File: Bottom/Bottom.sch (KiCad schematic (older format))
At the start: 41 parts, among them M1 Stepper_Motor_bipolar, M2 Stepper_Motor_bipolar, U1 GP2S60, U2 GP2S60, U7 DRV8833PWP, U8 DRV8833PWP

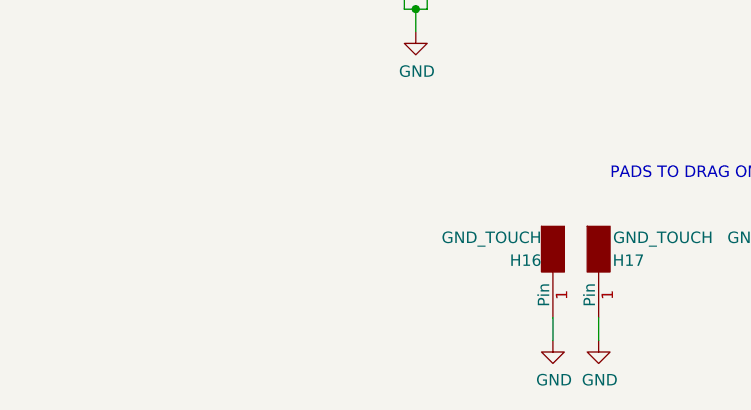
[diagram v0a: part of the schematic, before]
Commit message: finish top, changes to front, added graphic
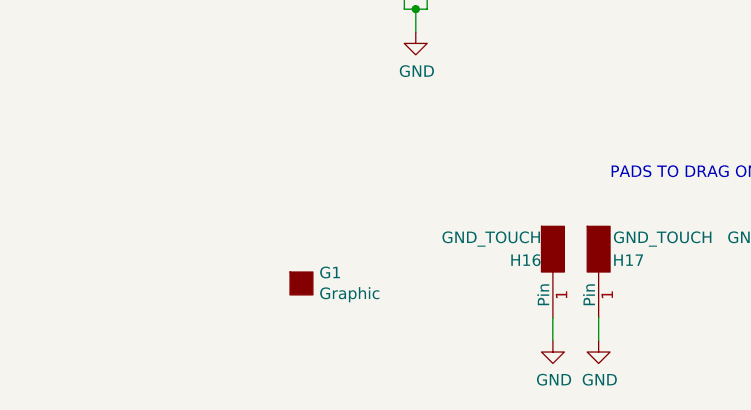
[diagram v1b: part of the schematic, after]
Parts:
- added G1: Graphic, Print:d2, symbol Custom:Graphic
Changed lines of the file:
@@
+	1    0    0    -1
+$EndComp
+$Comp
+L Custom:Graphic G1
+U 1 1 5DEDE762
+P 2450 7200
+F 0 "G1" H 2528 7246 50  0000 L CNN
+F 1 "Graphic" H 2528 7155 50  0000 L CNN
+F 2 "Print:d2" H 2300 7350 50  0001 C CNN
+F 3 "" H 2300 7350 50  0001 C CNN
+	1    2450 7200
 	1    0    0    -1
 $EndComp

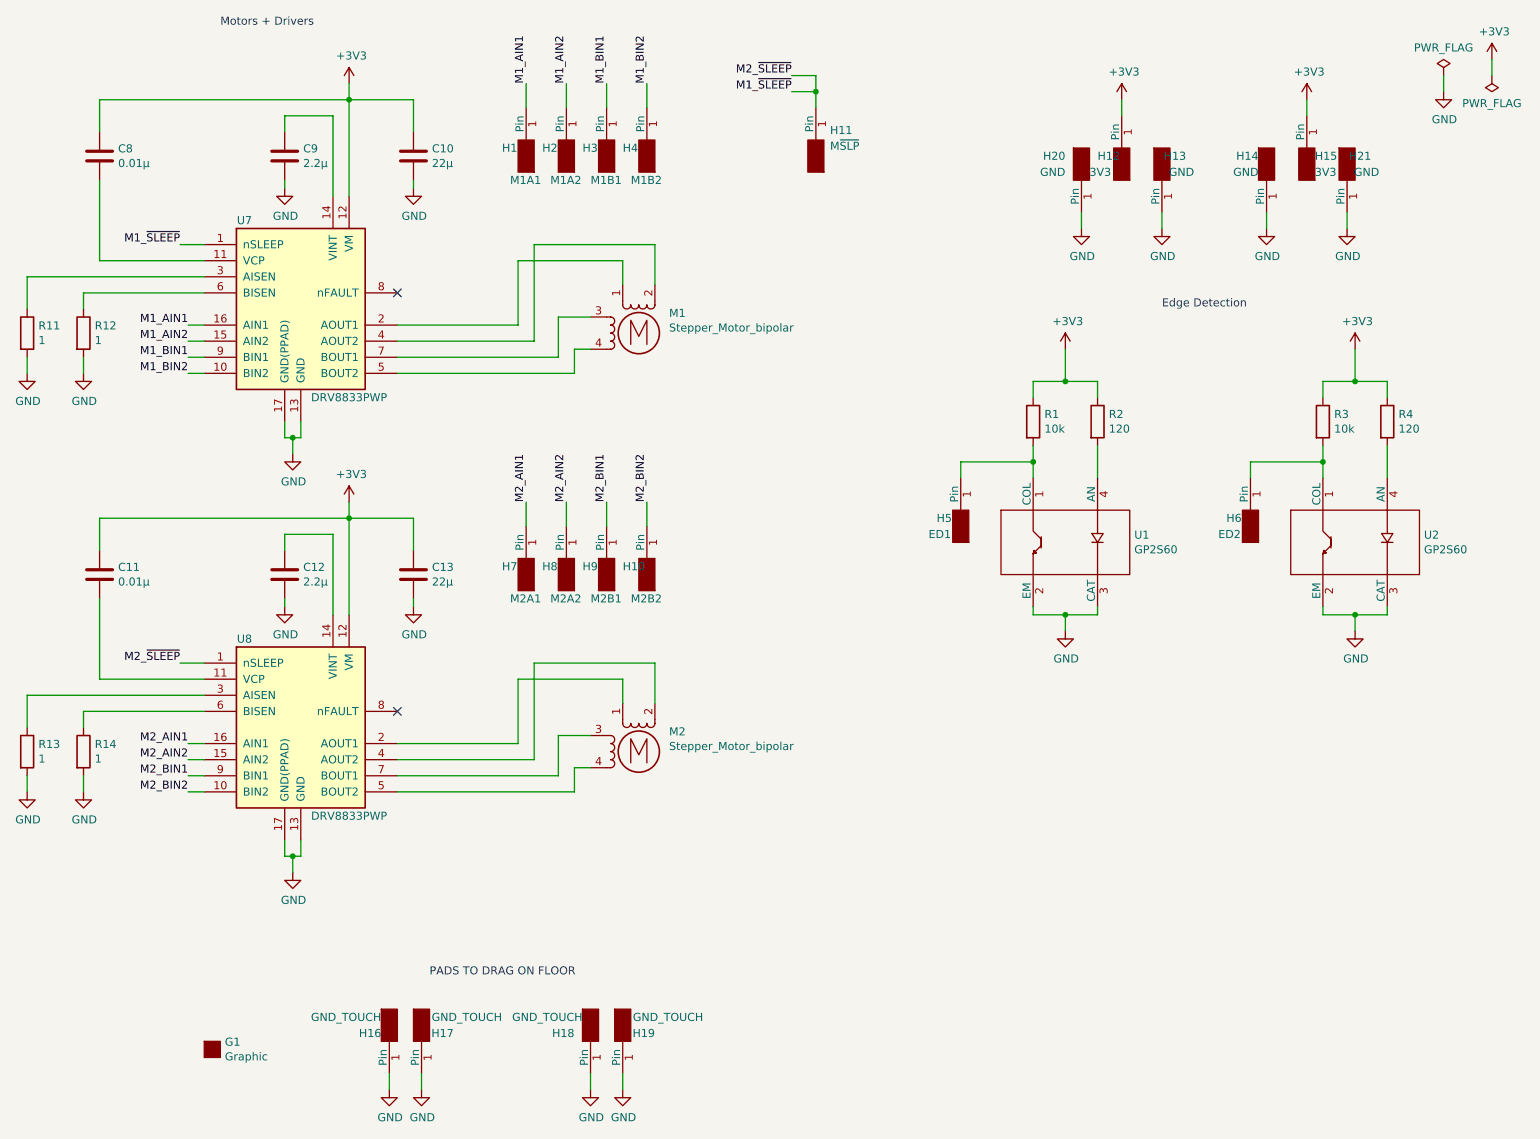
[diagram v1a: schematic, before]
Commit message: Bottom, new motor, positioning and start routing
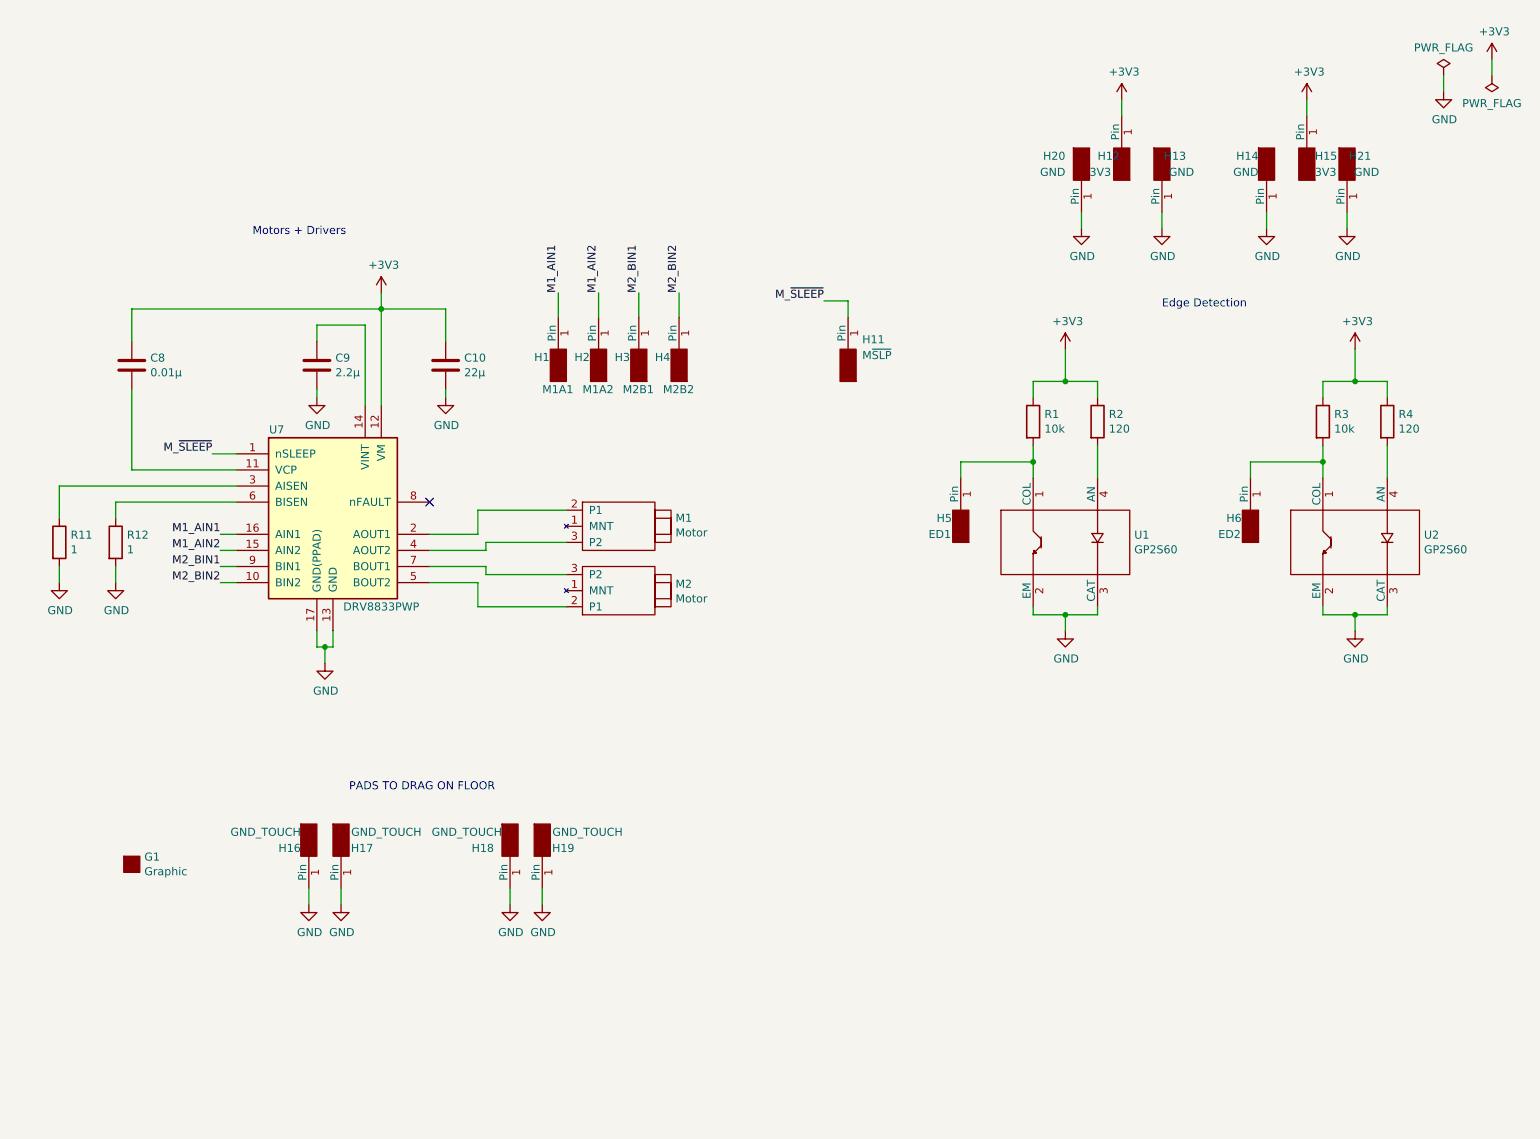
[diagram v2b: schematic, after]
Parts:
- removed C11: 0.01µ, Capacitor_SMD:C_0805_2012Metric, symbol Device:C
- removed C12: 2.2µ, Capacitor_SMD:C_0805_2012Metric, symbol Device:C
- removed C13: 22µ, Capacitor_SMD:C_0805_2012Metric, symbol Device:C
- removed H10: M2B2, Custom:Mounting_Pad_Signal, symbol Custom:MountingPad
- removed H7: M2A1, Custom:Mounting_Pad_Signal, symbol Custom:MountingPad
- removed H8: M2A2, Custom:Mounting_Pad_Signal, symbol Custom:MountingPad
- removed H9: M2B1, Custom:Mounting_Pad_Signal, symbol Custom:MountingPad
- removed M1, M2: Stepper_Motor_bipolar, Custom:Medium_Stepper, symbol Motor:Stepper_Motor_bipolar
- removed R13, R14: 1, Resistor_SMD:R_0805_2012Metric, symbol Device:R
- removed U8: DRV8833PWP, Package_SO:HTSSOP-16-1EP_4.4x5mm_P0.65mm_EP3.4x5mm_Mask2.46x2.31mm_ThermalVias, symbol Driver_Motor:DRV8833PWP
- added M1, M2: Motor, Custom:Small_DC_Motor, symbol Custom:Motor
- H3: value M1B1 -> M2B1
- H4: value M1B2 -> M2B2
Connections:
- net M1_BIN1 is gone; now on net M2_BIN1: H3.1 (Pin), U7.9 (BIN1)
- net M1_BIN2 is gone; now on net M2_BIN2: H4.1 (Pin), U7.10 (BIN2)
- net at U7.2 (AOUT1): now also M1.2 (P1)
- net at U7.4 (AOUT2): now also M1.3 (P2)
- net at U7.7 (BOUT1): now also M2.3 (P2)
- net at U7.5 (BOUT2): now also M2.2 (P1)
- net M1_~SLEEP renamed M_~SLEEP
- no-connect marks 2 -> 1
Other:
- moved on the sheet: C10, C8, C9, G1, H1, H11, H16, H17, H18, H19, H2, H3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
